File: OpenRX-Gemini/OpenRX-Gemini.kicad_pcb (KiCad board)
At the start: 2 copper layers, 0 parts

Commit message: Gemini: copy Mono schematic + PCB as starting point
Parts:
- added AE1: 2450AT18A100E, OpenRX-Shared:ANT-SMD_L3.2-W1.6, F.Cu at (111.0, 88.6)
- added C1: 100nF, Capacitor_SMD:C_0201_0603Metric, F.Cu at (108.1, 88.8)
- added C10: 1uF, Capacitor_SMD:C_0201_0603Metric, B.Cu at (111.5, 96.5)
- added C11: 10uF, Capacitor_SMD:C_0402_1005Metric, B.Cu at (112.2, 96.7)
- added C12: 10uF, Capacitor_SMD:C_0402_1005Metric, B.Cu at (109.2, 96.7)
- added C13: 10pF, Capacitor_SMD:C_0201_0603Metric, B.Cu at (111.7, 94.9)
- added C14: 1uF, Capacitor_SMD:C_0201_0603Metric, B.Cu at (107.1, 88.6)
- added C15: 220pF, Capacitor_SMD:C_0201_0603Metric, B.Cu at (108.3, 84.3)
- added C16: 0.3pF, Capacitor_SMD:C_0201_0603Metric, B.Cu at (105.3, 83.9)
- added C18: 100nF, Capacitor_SMD:C_0201_0603Metric, F.Cu at (108.6, 85.4)
- added C19: 1uF, Capacitor_SMD:C_0201_0603Metric, F.Cu at (111.6, 90.7)
- added C2: 100nF, Capacitor_SMD:C_0201_0603Metric, F.Cu at (108.6, 88.8)
- added C20: 4.7uF, Capacitor_SMD:C_0402_1005Metric, B.Cu at (110.6, 88.6)
- added C21: 100nF, Capacitor_SMD:C_0201_0603Metric, B.Cu at (111.2, 90.7)
- added C22: 100nF, Capacitor_SMD:C_0201_0603Metric, B.Cu at (108.1, 96.2)
- added C23: 100nF, Capacitor_SMD:C_0201_0603Metric, B.Cu at (112.3, 91.1)
- added C24: 100nF, Capacitor_SMD:C_0201_0603Metric, B.Cu at (105.9, 96.2)
- added C3: 100nF, Capacitor_SMD:C_0201_0603Metric, B.Cu at (104.7, 96.2)
- added C4: 100nF, Capacitor_SMD:C_0201_0603Metric, B.Cu at (105.3, 96.2)
- added C5: 100nF, Capacitor_SMD:C_0201_0603Metric, F.Cu at (104.7, 91.4)
- added C6: 18pF, Capacitor_SMD:C_0201_0603Metric, F.Cu at (112.7, 91.1)
- added C7: 18pF, Capacitor_SMD:C_0201_0603Metric, F.Cu at (111.7, 93.6)
- added C8: 1uF, Capacitor_SMD:C_0201_0603Metric, F.Cu at (106.4, 88.8)
- added C9: 1uF, Capacitor_SMD:C_0201_0603Metric, B.Cu at (110.4, 97.2)
- added D1: XL-1010RGBC-WS2812B, OpenRX-Shared:LED-SMD_4P-L1.0-W1.0-TL_XL-1010RGBC-WS2812B, F.Cu at (108.6, 84.3)
- added JP1: U.FL-R-SMT-1(80), OpenRX-Shared:RF-SMD_FRF05002-JSS103M, F.Cu at (110.7, 85.4)
- added L1: 10uH, Inductor_SMD:L_0603_1608Metric, B.Cu at (106.8, 96.9)
- added L2: 24nH, Inductor_SMD:L_0201_0603Metric, F.Cu at (111.6, 91.5)
- added R1: 10k, Resistor_SMD:R_0201_0603Metric, F.Cu at (107.0, 88.8)
- added R2: 10k, Resistor_SMD:R_0201_0603Metric, B.Cu at (105.0, 89.5)
- added R3: 10k, Resistor_SMD:R_0201_0603Metric, F.Cu at (104.6, 93.2)
- added R4: 10k, Resistor_SMD:R_0201_0603Metric, F.Cu at (107.5, 88.8)
- added R6: 220R, Resistor_SMD:R_0201_0603Metric, B.Cu at (111.7, 94.4)
- added T1: 0900PC16J0042001E, OpenRX-Shared:FILTER-SMD_10P-L2.0-W1.6-BL, B.Cu at (108.8, 88.3)
- added TP1: RX, OpenRX-Shared:SolderPad_1.2x2.0mm, F.Cu at (104.9, 97.6)
- added TP2: TX, OpenRX-Shared:SolderPad_1.2x2.0mm, F.Cu at (107.6, 97.6)
- added TP3: 5V, OpenRX-Shared:SolderPad_1.2x2.0mm, F.Cu at (109.8, 97.6)
- added TP4: GND, OpenRX-Shared:SolderPad_1.2x2.0mm, F.Cu at (112.5, 97.6)
- added U1: ESP32-C3FH4, OpenRX-Shared:QFN-32_L5.0-W5.0-P0.50-TL-EP3.7, F.Cu at (107.8, 92.5)
- added U2: TLV75533PDQNR, OpenRX-Shared:X2SON-4_L1.0-W1.0-P0.65-TL-EP, B.Cu at (110.4, 96.3)
- added U3: TS2306A 240GF MSM 9_C2976675, OpenRX-Shared:SW-SMD_4P-L3.0-W2.0-P0.85-LS3.5, F.Cu at (105.3, 85.4)
- added U4: LR1121IMLTRT, OpenRX-Shared:QFN-32_L5.0-W5.0-P0.50-BL-EP3.7, B.Cu at (107.8, 92.5)
- added U5: OW7EL89CENUYO3YLC-32M, OpenRX-Shared:OSC-SMD_4P-L2.0-W1.6-BL_TXC_7Z, B.Cu at (112.1, 92.7)
- added U6: SKY13588-460LF, OpenRX-Shared:QFN-12_L2.0-W2.0-P0.50-BL-EP0.8, B.Cu at (109.2, 85.9)
- added U7: RFX2401C, OpenRX-Shared:QFN-16_L3.0-W3.0-P0.50-BL-EP1.7, B.Cu at (106.1, 86.0)
- added USB2: DEA102700LT-6307A2, OpenRX-Shared:FILTER-SMD_4P-L1.0-W0.5-L_DEA102700LT-XXX, B.Cu at (106.0, 88.7)
- added X1: CJ17-400001010B20, OpenRX-Shared:CRYSTAL-SMD_4P-L1.6-W1.2-BL, F.Cu at (112.0, 92.5)
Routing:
- net +3V3: track 0.00 -> 3.84 mm
- net Net-(U4-VTCXO): track 0.00 -> 2.11 mm
- net Net-(U6-J2): track 0.00 -> 1.68 mm
- net Net-(U5-OUTPUT): track 0.00 -> 0.83 mm
- net GND: track 0.00 -> 0.79 mm
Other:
- board outline added: 9 x 15.4 mm
- copper layers 2 -> 4

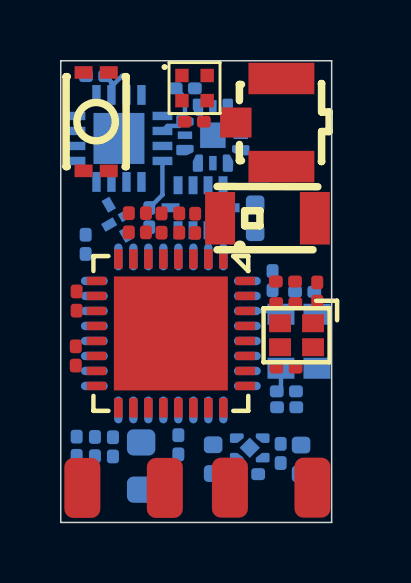
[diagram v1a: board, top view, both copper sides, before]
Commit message: Copy Gemini PCB layout to Mono
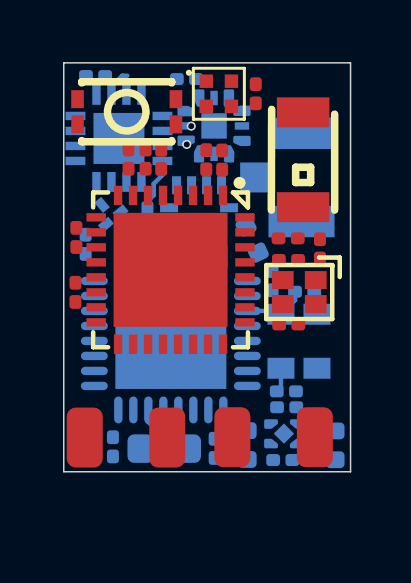
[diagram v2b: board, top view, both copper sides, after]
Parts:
- JP1: moved to B.Cu
- moved C1 2.29 mm to (109.0, 86.7)
- moved C2 2.29 mm to (109.5, 86.7)
- moved AE1 2.28 mm to (112.2, 86.7), turned to 90 degrees
- moved C18 2.25 mm to (110.6, 84.5), turned to -90 degrees
- moved R4 2.12 mm to (107.5, 86.7)
- moved C5 2.12 mm to (104.7, 89.3)
- moved C8 2.12 mm to (106.4, 86.7)
- moved R1 2.12 mm to (107.0, 86.7)
- moved R3 2.12 mm to (104.6, 91.1)
- moved U1 2.12 mm to (107.8, 90.3)
- moved JP1 1.95 mm to (111.4, 87.3), turned to 90 degrees
- moved TP1 1.68 mm to (104.9, 95.9)
- moved TP2 1.68 mm to (107.7, 95.9)
- moved TP3 1.68 mm to (109.9, 95.9)
- moved TP4 1.68 mm to (112.6, 95.9)
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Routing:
- net +3V3: track 3.84 -> 1.75 mm
- net Net-(U4-DCC_SW): track 0.00 -> 2.07 mm
- net /ESP32-C3 + LR1121 Mono/DIO8-1: track 0.00 -> 0.17 mm, vias 0 -> 1
- net /ESP32-C3 + LR1121 Mono/DIO7-1: track 0.00 -> 0.13 mm, vias 0 -> 1
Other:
- board size 9 x 15.4 mm -> 9.6 x 13.6 mm

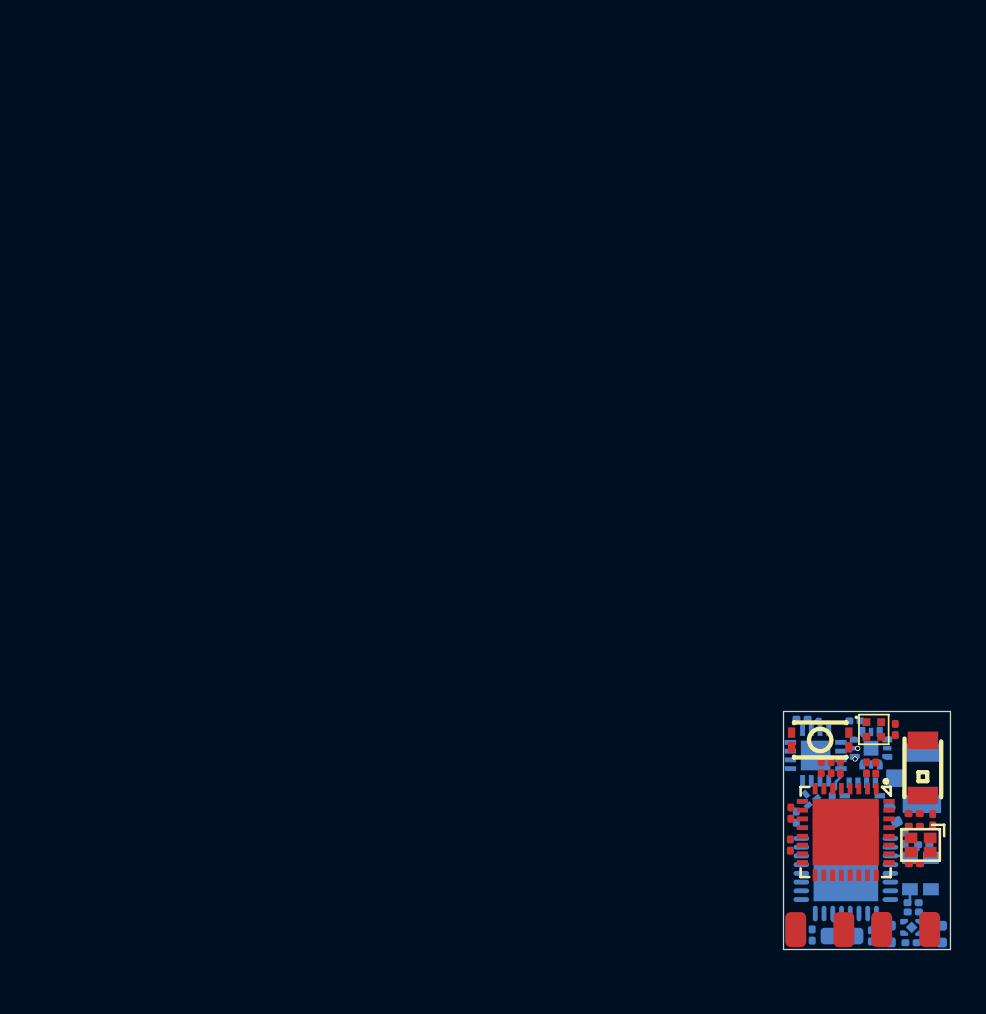
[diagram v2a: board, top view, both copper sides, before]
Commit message: Apply JLCPCB 6-layer advanced DRC rules to Mono and Gemini
Rules applied:
- Min clearance: 0.09mm (3.5mil)
- Min track width: 0.09mm (3.5mil)
- Min via diameter: 0.25mm
- Min via drill: 0.15mm
- Min annular ring: 0.05mm
- Min hole-to-hole: 0.25mm
- Default net class clearance: 0.09mm (was 0.2mm — this was the override)
- Default track width: 0.1mm
- Zone clearance: 0.09mm (was 0.5mm)
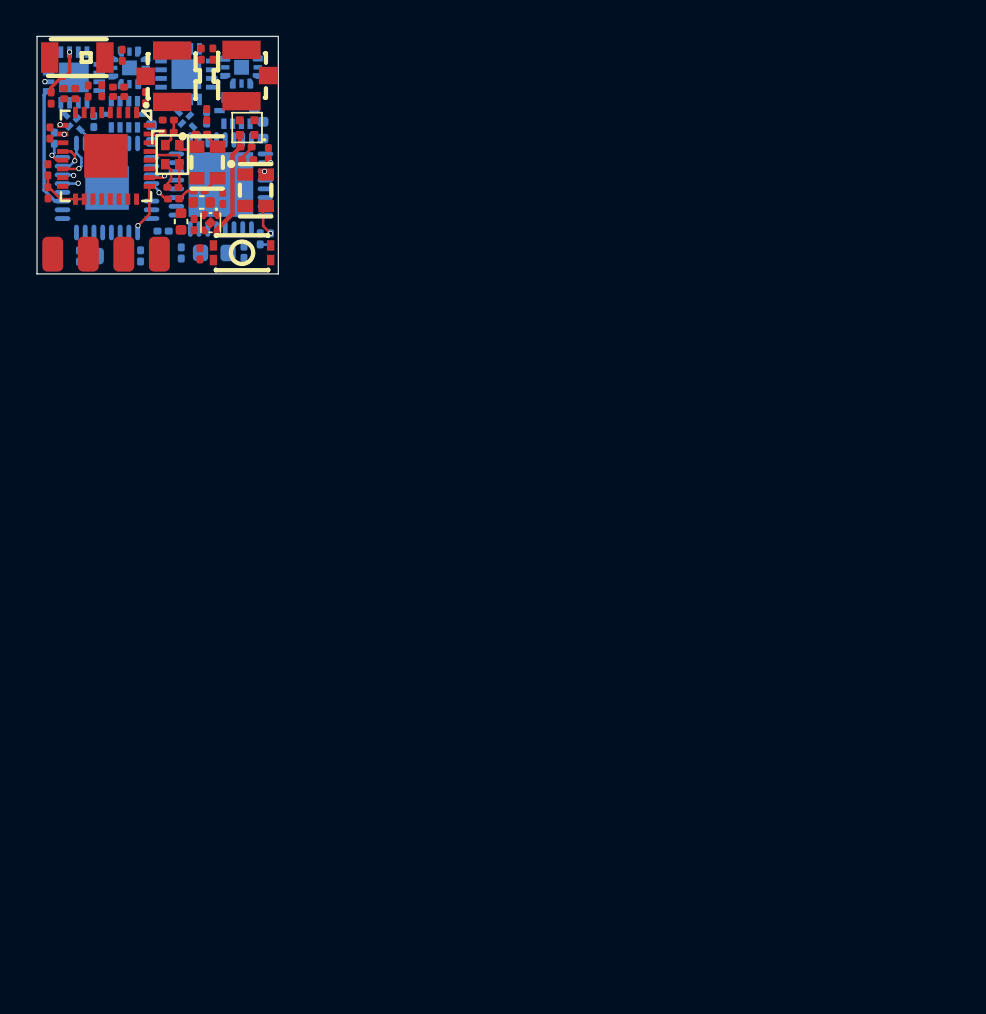
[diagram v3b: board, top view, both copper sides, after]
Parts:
- added C17: 10pF, Capacitor_SMD:C_0201_0603Metric, B.Cu at (74.3, 56.4)
- added C25: 100nF, Capacitor_SMD:C_0201_0603Metric, F.Cu at (74.7, 51.5)
- added C26: 100nF, Capacitor_SMD:C_0201_0603Metric, F.Cu at (73.6, 51.8)
- added C27: 100nF, Capacitor_SMD:C_0201_0603Metric, B.Cu at (73.3, 57.1)
- added C28: 4.7uF, Capacitor_SMD:C_0402_1005Metric, B.Cu at (74.4, 50.1)
- added C29: 100nF, Capacitor_SMD:C_0201_0603Metric, B.Cu at (69.8, 57.2)
- added C30: 0.3pF, Capacitor_SMD:C_0201_0603Metric, F.Cu at (70.9, 45.8)
- added C31: 220pF, Capacitor_SMD:C_0201_0603Metric, B.Cu at (71.2, 49.5)
- added C32: 1uF, Capacitor_SMD:C_0201_0603Metric, F.Cu at (71.6, 45.8)
- added JP2: U.FL-R-SMT-1(80), OpenRX-Shared:RF-SMD_FRF05002-JSS103M, F.Cu at (74.0, 47.0)
- added L3: 10uH, Inductor_SMD:L_0603_1608Metric, B.Cu at (71.6, 57.2)
- added R5: 10k, Resistor_SMD:R_0201_0603Metric, F.Cu at (65.2, 47.9)
- added R7: 220R, Resistor_SMD:R_0201_0603Metric, B.Cu at (74.9, 56.4)
- added R8: 10k, Resistor_SMD:R_0201_0603Metric, B.Cu at (68.7, 55.9)
- added T2: 0900PC16J0042001E, OpenRX-Shared:FILTER-SMD_10P-L2.0-W1.6-BL, B.Cu at (72.9, 49.0)
- added U10: RFX2401C, OpenRX-Shared:QFN-16_L3.0-W3.0-P0.50-BL-EP1.7, B.Cu at (70.0, 46.9)
- added U11: SKY13588-460LF, OpenRX-Shared:QFN-12_L2.0-W2.0-P0.50-BL-EP0.8, B.Cu at (73.2, 46.5)
- added U8: OW7EL89CENUYO3YLC-32M, OpenRX-Shared:OSC-SMD_4P-L2.0-W1.6-BL_TXC_7Z, F.Cu at (74.0, 53.6)
- added U9: LR1121IMLTRT, OpenRX-Shared:QFN-32_L5.0-W5.0-P0.50-BL-EP3.7, B.Cu at (72.0, 53.3)
- added USB3: DEA102700LT-6307A2, OpenRX-Shared:FILTER-SMD_4P-L1.0-W0.5-L_DEA102700LT-XXX, B.Cu at (70.0, 49.5)
- C10, C11, C12, C13, C14, C16, C21, C23, C3, C4, C9, JP1, R6, U2, U5: moved to F.Cu
- moved AE1 63.2 mm to (63.8, 46.0), turned to 180 degrees
- moved C4 62.3 mm to (66.2, 47.7), turned to 0 degrees
- moved TP4 60.2 mm to (66.5, 57.2), turned to 180 degrees
- moved C19 60.2 mm to (67.7, 48.3), turned to 90 degrees
- moved C3 60.1 mm to (62.1, 53.7)
- moved C11 59.6 mm to (70.9, 54.3), turned to 180 degrees
- moved C6 59.3 mm to (69.0, 49.6), turned to 180 degrees
- moved C14 59.0 mm to (66.4, 45.9), turned to 90 degrees
- moved C13 58.8 mm to (69.3, 54.1)
- moved JP1 58.8 mm to (68.5, 47.1), turned to -90 degrees
- moved R1 58.4 mm to (63.4, 47.8), turned to 180 degrees
- moved L2 58.4 mm to (69.0, 50.3)
- moved X1 58.3 mm to (69.2, 51.5), turned to -90 degrees
- moved C10 58.3 mm to (72.1, 54.1), turned to 90 degrees
- moved C9 58.1 mm to (70.5, 55.6), turned to 90 degrees
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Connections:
- net /ESP32-C3 + LR1121 Mono/BUTTON renamed /ESP32-C3 + 2x LR1121 Gemini/BUTTON
- net /ESP32-C3 + LR1121 Mono/CHIP_EN renamed /ESP32-C3 + 2x LR1121 Gemini/CHIP_EN
- net /ESP32-C3 + LR1121 Mono/MISO renamed /ESP32-C3 + 2x LR1121 Gemini/MISO
- net /ESP32-C3 + LR1121 Mono/MOSI renamed /ESP32-C3 + 2x LR1121 Gemini/MOSI
- net /ESP32-C3 + LR1121 Mono/NSS1 renamed /ESP32-C3 + 2x LR1121 Gemini/NSS2
- net /ESP32-C3 + LR1121 Mono/RXEN renamed /ESP32-C3 + 2x LR1121 Gemini/RXEN2
- net /ESP32-C3 + LR1121 Mono/SCK renamed /ESP32-C3 + 2x LR1121 Gemini/SCK
- net /ESP32-C3 + LR1121 Mono/TXEN renamed /ESP32-C3 + 2x LR1121 Gemini/TXEN2
- net /ESP32-C3 + LR1121 Mono/WIFI renamed /ESP32-C3 + 2x LR1121 Gemini/WIFI
- net /ESP32-C3 + LR1121 Mono/XTAL_N renamed /ESP32-C3 + 2x LR1121 Gemini/XTAL_N
- net /ESP32-C3 + LR1121 Mono/XTAL_P renamed /ESP32-C3 + 2x LR1121 Gemini/XTAL_P
- D1 pad 4: /ESP32-C3 + LR1121 Mono/LED -> /ESP32-C3 + 2x LR1121 Gemini/LED
- R4 pad 2: /ESP32-C3 + LR1121 Mono/RST1 -> /ESP32-C3 + 2x LR1121 Gemini/RST1
- U1 pad 14: /ESP32-C3 + LR1121 Mono/LED -> /ESP32-C3 + 2x LR1121 Gemini/BUSY2
- U1 pad 16: unconnected-(U1-GPIO10-Pad16) -> /ESP32-C3 + 2x LR1121 Gemini/RST2
- U1 pad 25: unconnected-(U1-GPIO18-Pad25) -> /ESP32-C3 + 2x LR1121 Gemini/IRQ2
- U1 pad 26: unconnected-(U1-GPIO19-Pad26) -> /ESP32-C3 + 2x LR1121 Gemini/LED
- U1 pad 4: unconnected-(U1-XTAL_32K_P-Pad4) -> /ESP32-C3 + 2x LR1121 Gemini/NSS1
- U1 pad 5: /ESP32-C3 + LR1121 Mono/IRQ1 -> /ESP32-C3 + 2x LR1121 Gemini/IRQ1
- U1 pad 6: /ESP32-C3 + LR1121 Mono/RST1 -> /ESP32-C3 + 2x LR1121 Gemini/RST1
- U1 pad 8: /ESP32-C3 + LR1121 Mono/BUSY1 -> /ESP32-C3 + 2x LR1121 Gemini/BUSY1
- U4 pad 10: /ESP32-C3 + LR1121 Mono/DIO8-1 -> /ESP32-C3 + 2x LR1121 Gemini/DIO8-2
- U4 pad 11: /ESP32-C3 + LR1121 Mono/DIO7-1 -> /ESP32-C3 + 2x LR1121 Gemini/DIO7-2
- U4 pad 25: /ESP32-C3 + LR1121 Mono/BUSY1 -> /ESP32-C3 + 2x LR1121 Gemini/BUSY2
- U4 pad 6: /ESP32-C3 + LR1121 Mono/RST1 -> /ESP32-C3 + 2x LR1121 Gemini/RST2
- U4 pad 9: /ESP32-C3 + LR1121 Mono/IRQ1 -> /ESP32-C3 + 2x LR1121 Gemini/IRQ2
- U6 pad 4: /ESP32-C3 + LR1121 Mono/DIO7-1 -> /ESP32-C3 + 2x LR1121 Gemini/DIO7-1
- U6 pad 5: /ESP32-C3 + LR1121 Mono/DIO8-1 -> /ESP32-C3 + 2x LR1121 Gemini/DIO8-1
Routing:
- net /ESP32-C3 + 2x LR1121 Gemini/TXEN2: track 0.00 -> 7.13 mm
- net +5V: track 0.00 -> 6.05 mm
- net /ESP32-C3 + 2x LR1121 Gemini/XTAL_N: track 0.00 -> 3.63 mm
- net GND: track 0.79 -> 4.31 mm
- net /ESP32-C3 + 2x LR1121 Gemini/BUSY2: track 0.00 -> 2.55 mm, vias 0 -> 1
- net /ESP32-C3 + 2x LR1121 Gemini/IRQ2: track 0.00 -> 2.52 mm, vias 0 -> 1
- net /ESP32-C3 + 2x LR1121 Gemini/NSS2: track 0.00 -> 2.11 mm, vias 0 -> 1
- net Net-(U4-DCC_SW): track 2.07 -> 0.00 mm
- net /ESP32-C3 + 2x LR1121 Gemini/SCK: track 0.00 -> 1.93 mm, vias 0 -> 1
- net Net-(U8-OUTPUT): track 0.00 -> 1.72 mm, vias 0 -> 1
- net +3V3: track 1.75 -> 3.43 mm, vias 0 -> 1
- net Net-(C6-Pad1): track 0.00 -> 1.63 mm
- net Net-(U4-XTA): track 0.00 -> 1.36 mm, vias 0 -> 1
- net Net-(U6-J2): track 1.68 -> 2.85 mm, vias 0 -> 1
- net Net-(U4-VTCXO): track 2.11 -> 0.97 mm
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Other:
- board size 9.6 x 13.6 mm -> 13.8 x 13.6 mm
- copper layers 4 -> 6

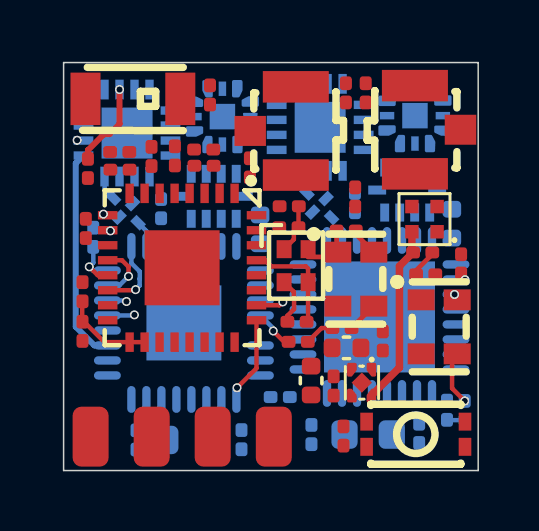
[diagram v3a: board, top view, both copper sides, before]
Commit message: Repo cleanup: final state for handoff
- Clean README with architecture, BOM, CE notes, status
- Remove dated analysis files (absorbed into FINAL_NETLIST + KICAD_WORKFLOW)
- Remove stale OpenRX-Dual (archived), ERC reports, backups, prl files
- Updated .gitignore for .kicad_dru, production backups
- CERN-OHL-S v2 license confirmed
- 3 active projects: Lite, Mono, Gemini
- Schematics final, initial PCB layouts done, routing in progress
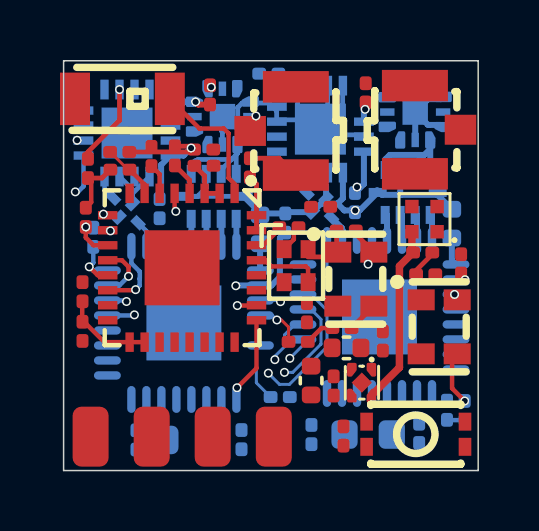
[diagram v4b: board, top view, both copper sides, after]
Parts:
- C21, C30: moved to B.Cu
- moved C30 2.65 mm to (68.3, 45.1), turned to 180 degrees
- moved C21 2.49 mm to (68.9, 50.1), turned to 90 degrees
- moved C6 1.05 mm to (70.1, 49.6), turned to 0 degrees
- moved C7 0.45 mm to (69.6, 53.1), turned to -90 degrees
- moved C5 0.37 mm to (62.2, 49.9)
- moved AE1 0.35 mm to (63.5, 46.0)
- moved U11 0.12 mm to (73.2, 46.4)
- moved T2 0.08 mm to (73.0, 49.1)
- moved U10 0.06 mm to (70.0, 47.0)
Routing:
- net GND: track 4.31 -> 41.1 mm, vias 0 -> 2
- net +3V3: track 3.43 -> 21.3 mm, vias 1 -> 7
- net /ESP32-C3 + 2x LR1121 Gemini/TXEN2: track 7.13 -> 1.38 mm, vias 0 -> 1
- net /ESP32-C3 + 2x LR1121 Gemini/MOSI: track 0.81 -> 5.67 mm, vias 2 -> 3
- net /ESP32-C3 + 2x LR1121 Gemini/WIFI: track 0.00 -> 4.52 mm
- net Net-(T1-RX): track 0.00 -> 3.94 mm
- net Net-(T2-RX): track 0.00 -> 3.92 mm
- net /ESP32-C3 + 2x LR1121 Gemini/MISO: track 1.01 -> 4.18 mm, vias 2 -> 3
- net /ESP32-C3 + 2x LR1121 Gemini/RST2: track 0.00 -> 1.97 mm
- net /ESP32-C3 + 2x LR1121 Gemini/CHIP_EN: track 0.00 -> 1.89 mm
- net /ESP32-C3 + 2x LR1121 Gemini/RXEN1: track 0.00 -> 1.72 mm, vias 0 -> 1
- net /ESP32-C3 + 2x LR1121 Gemini/XTAL_N: track 3.63 -> 2.29 mm
- net Net-(U4-VTCXO): track 0.97 -> 2.13 mm, vias 0 -> 2
- net /ESP32-C3 + 2x LR1121 Gemini/NSS1: track 0.00 -> 1.13 mm
- net /ESP32-C3 + 2x LR1121 Gemini/BUSY1: track 0.00 -> 1.10 mm, vias 0 -> 1
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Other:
- board size 13.8 x 13.6 mm -> 13.8 x 13.7 mm
